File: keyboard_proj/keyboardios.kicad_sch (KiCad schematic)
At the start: 23 parts

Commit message: Tous les schematics vérifiés 1x
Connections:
- net PB0: now also J?.19 (Pin_19); no longer J?.17 (Pin_17)
- net PB2: now also J?.17 (Pin_17); no longer J?.19 (Pin_19)
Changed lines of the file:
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@@
     )
   )
-  (global_label "PB0" (shape input) (at 154.94 129.54 90) (fields_autoplaced)
+  (global_label "PB0" (shape input) (at 149.86 129.54 90) (fields_autoplaced)
     (effects (font (size 1.27 1.27)) (justify left))
-    (property "Intersheet References" "${INTERSHEET_REFS}" (id 0) (at 155.0194 123.3774 90)
+    (property "Intersheet References" "${INTERSHEET_REFS}" (id 0) (at 149.9394 123.3774 90)
       (effects (font (size 1.27 1.27)) (justify left) hide)
     )
@@
     )
   )
-  (global_label "PB2" (shape input) (at 149.86 129.54 90) (fields_autoplaced)
+  (global_label "PB2" (shape input) (at 154.94 129.54 90) (fields_autoplaced)
     (effects (font (size 1.27 1.27)) (justify left))
-    (property "Intersheet References" "${INTERSHEET_REFS}" (id 0) (at 149.9394 123.3774 90)
+    (property "Intersheet References" "${INTERSHEET_REFS}" (id 0) (at 155.0194 123.3774 90)
       (effects (font (size 1.27 1.27)) (justify left) hide)
     )

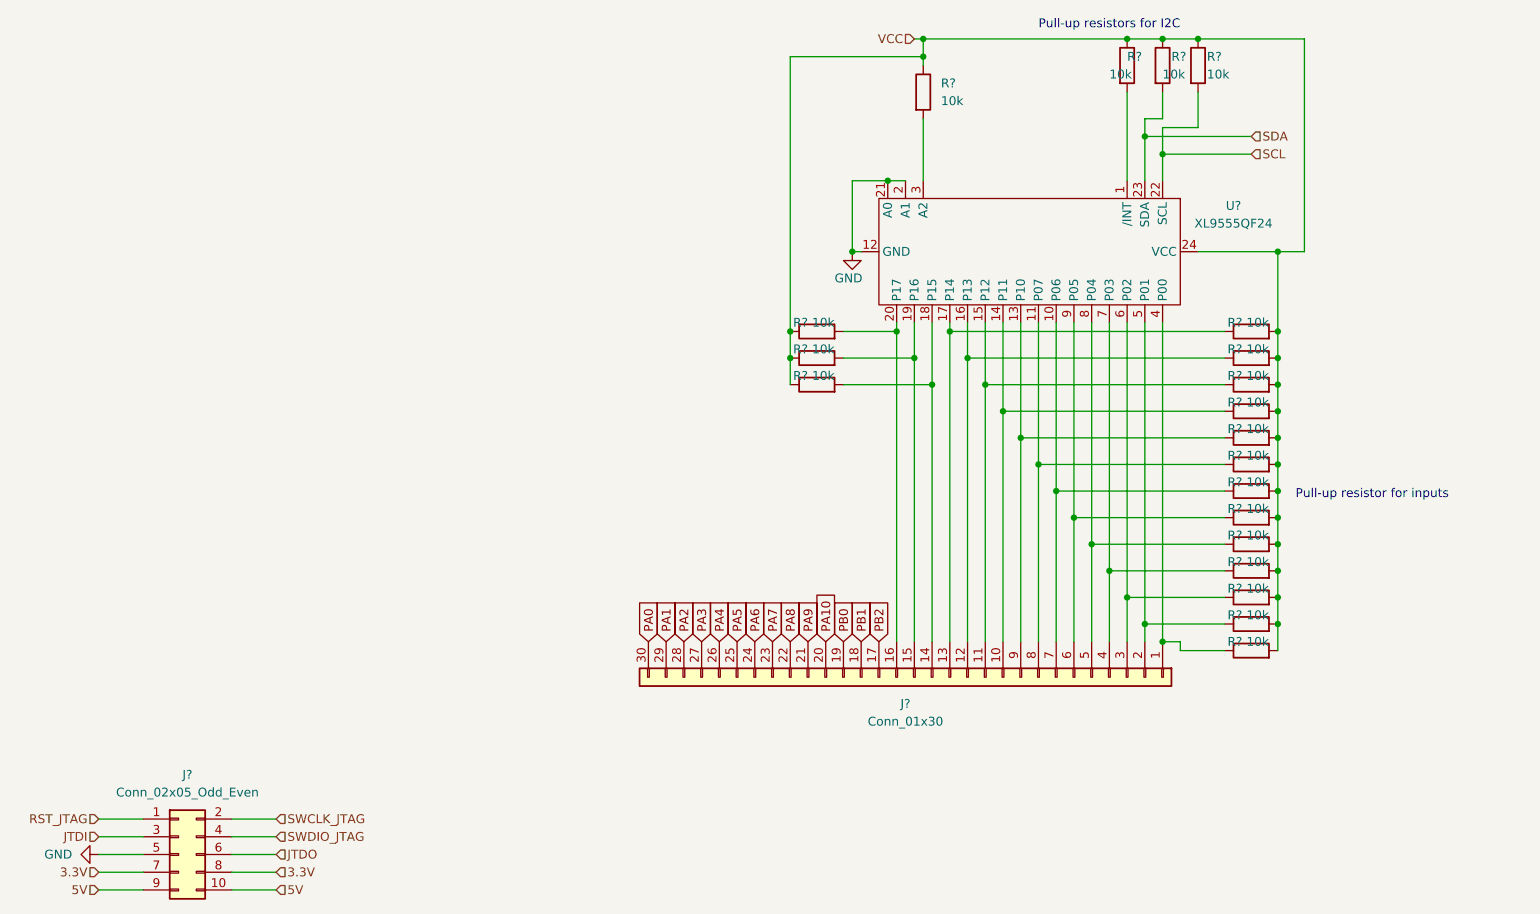
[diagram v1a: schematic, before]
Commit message: Ajout backlight et light sensor (in progress)
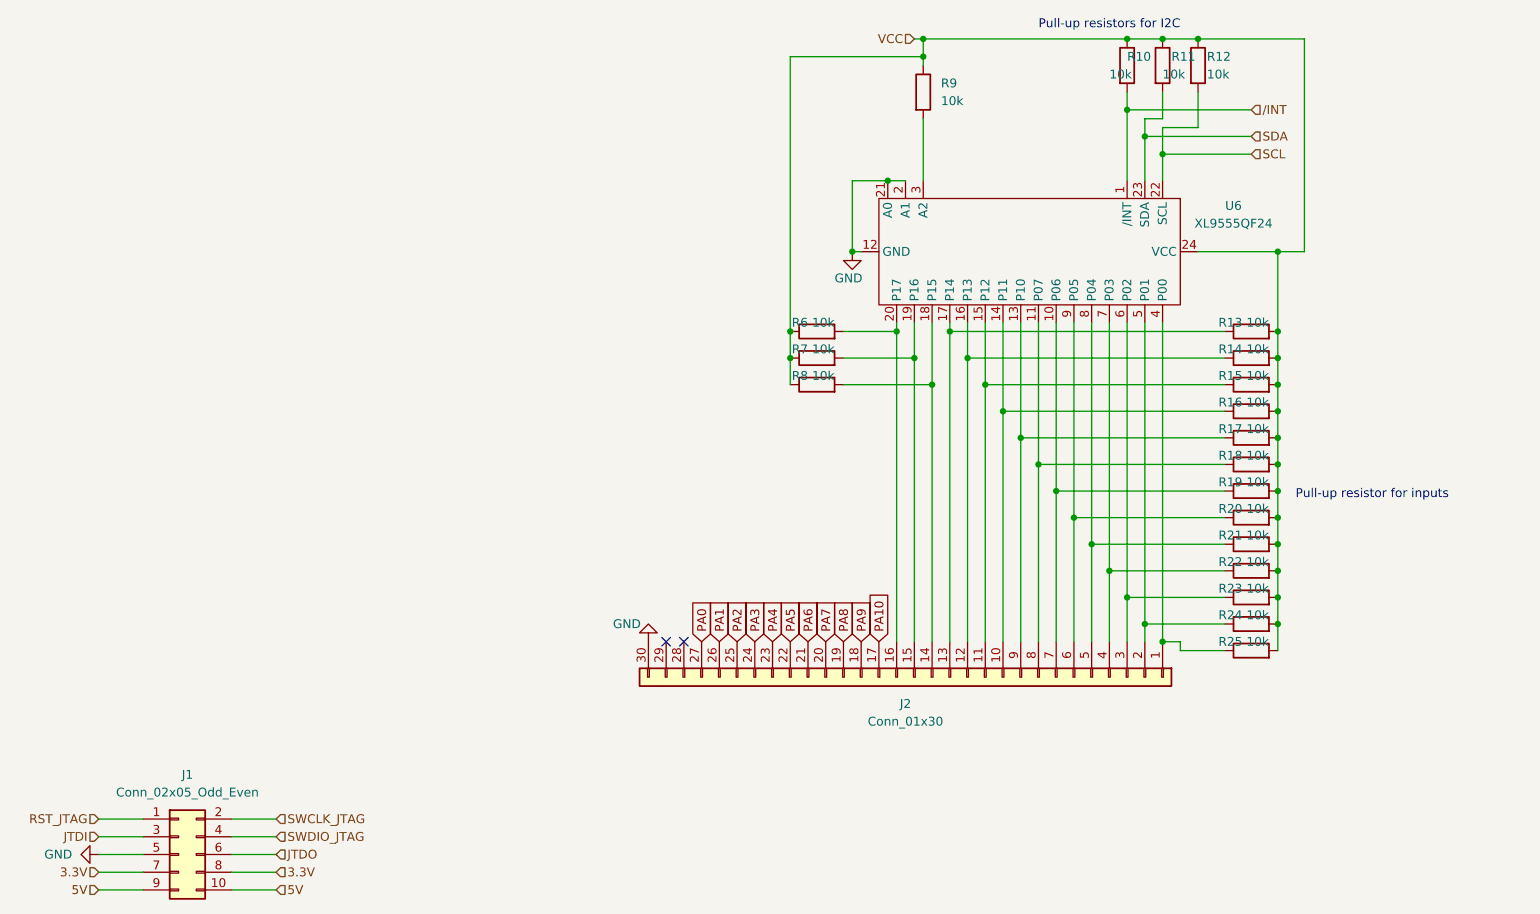
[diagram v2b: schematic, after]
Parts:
- gave numbers to parts that had none: 23
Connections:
- net PB0 is gone; now on net PA8: J2.19 (Pin_19)
- net PB1 is gone; now on net PA9: J2.18 (Pin_18)
- net PB2 is gone; now on net PA10: J2.17 (Pin_17)
- net GND: now also J2.30 (Pin_30)
- net PA0: now also J2.27 (Pin_27); no longer J2.30 (Pin_30)
- net PA1: now also J2.26 (Pin_26); no longer J2.29 (Pin_29)
- net PA10: no longer J2.20 (Pin_20)
- net PA2: now also J2.25 (Pin_25); no longer J2.28 (Pin_28)
- net PA3: now also J2.24 (Pin_24); no longer J2.27 (Pin_27)
- net PA4: now also J2.23 (Pin_23); no longer J2.26 (Pin_26)
- net PA5: now also J2.22 (Pin_22); no longer J2.25 (Pin_25)
- net PA6: now also J2.21 (Pin_21); no longer J2.24 (Pin_24)
- net PA7: now also J2.20 (Pin_20); no longer J2.23 (Pin_23)
- net PA8: no longer J2.22 (Pin_22)
- net PA9: no longer J2.21 (Pin_21)
- net /INT: now reaches R10.2, U6.1 (/INT)
- no-connect marks 0 -> 2

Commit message: Ajout des empreintes, il en manque encore
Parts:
- R10, R11, R12, R13, R14, R15, R16, R17, R18, R19, R20, R21, R22, R23, R24, R25, R6, R7, R8, R9: footprint (none) -> Resistor_SMD:R_0402_1005Metric
- U6: footprint (none) -> Package_DFN_QFN:QFN-24-1EP_4x4mm_P0.5mm_EP2.7x2.7mm
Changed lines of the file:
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@@
       (effects (font (size 1.27 1.27)) (justify left))
     )
-    (property "Footprint" "" (id 2) (at 193.802 46.99 90)
+    (property "Footprint" "Resistor_SMD:R_0402_1005Metric" (id 2) (at 193.802 46.99 90)
       (effects (font (size 1.27 1.27)) hide)
     )
@@
       (effects (font (size 1.27 1.27)) (justify left))
     )
-    (property "Footprint" "" (id 2) (at 208.28 102.108 90)
+    (property "Footprint" "Resistor_SMD:R_0402_1005Metric" (id 2) (at 208.28 102.108 90)
       (effects (font (size 1.27 1.27)) hide)
     )
@@
       (effects (font (size 1.27 1.27)) (justify left))
     )
-    (property "Footprint" "" (id 2) (at 188.722 46.99 90)
+    (property "Footprint" "Resistor_SMD:R_0402_1005Metric" (id 2) (at 188.722 46.99 90)
       (effects (font (size 1.27 1.27)) hide)
     )
@@
       (effects (font (size 1.27 1.27)) (justify left))
     )
-    (property "Footprint" "" (id 2) (at 208.28 98.298 90)
+    (property "Footprint" "Resistor_SMD:R_0402_1005Metric" (id 2) (at 208.28 98.298 90)
       (effects (font (size 1.27 1.27)) hide)
     )
@@
       (effects (font (size 1.27 1.27)) (justify left))
     )
-    (property "Footprint" "" (id 2) (at 159.512 50.8 90)
+    (property "Footprint" "Resistor_SMD:R_0402_1005Metric" (id 2) (at 159.512 50.8 90)
       (effects (font (size 1.27 1.27)) hide)
     )
@@
       (effects (font (size 1.27 1.27)) (justify left))
     )
-    (property "Footprint" "" (id 2) (at 208.28 94.488 90)
+    (property "Footprint" "Resistor_SMD:R_0402_1005Metric" (id 2) (at 208.28 94.488 90)
       (effects (font (size 1.27 1.27)) hide)
     )
@@
       (effects (font (size 1.27 1.27)) (justify left))
     )
-    (property "Footprint" "" (id 2) (at 208.28 86.868 90)
+    (property "Footprint" "Resistor_SMD:R_0402_1005Metric" (id 2) (at 208.28 86.868 90)
       (effects (font (size 1.27 1.27)) hide)
     )
@@
       (effects (font (size 1.27 1.27)) (justify left))
     )
-    (property "Footprint" "" (id 2) (at 208.28 121.158 90)
+    (property "Footprint" "Resistor_SMD:R_0402_1005Metric" (id 2) (at 208.28 121.158 90)
       (effects (font (size 1.27 1.27)) hide)
     )
@@
       (effects (font (size 1.27 1.27)) (justify left))
     )
-    (property "Footprint" "" (id 2) (at 208.28 132.588 90)
+    (property "Footprint" "Resistor_SMD:R_0402_1005Metric" (id 2) (at 208.28 132.588 90)
       (effects (font (size 1.27 1.27)) hide)
     )
@@
       (effects (font (size 1.27 1.27)) (justify left))
     )
-    (property "Footprint" "" (id 2) (at 208.28 90.678 90)
+    (property "Footprint" "Resistor_SMD:R_0402_1005Metric" (id 2) (at 208.28 90.678 90)
       (effects (font (size 1.27 1.27)) hide)
     )
@@
       (effects (font (size 1.27 1.27)) (justify left))
     )
-    (property "Footprint" "" (id 2) (at 208.28 109.728 90)
+    (property "Footprint" "Resistor_SMD:R_0402_1005Metric" (id 2) (at 208.28 109.728 90)
       (effects (font (size 1.27 1.27)) hide)
     )
@@
       (effects (font (size 1.27 1.27)) (justify left))
     )
-    (property "Footprint" "" (id 2) (at 208.28 117.348 90)
+    (property "Footprint" "Resistor_SMD:R_0402_1005Metric" (id 2) (at 208.28 117.348 90)
       (effects (font (size 1.27 1.27)) hide)
     )
@@
       (effects (font (size 1.27 1.27)) (justify left))
     )
-    (property "Footprint" "" (id 2) (at 208.28 113.538 90)
+    (property "Footprint" "Resistor_SMD:R_0402_1005Metric" (id 2) (at 208.28 113.538 90)
       (effects (font (size 1.27 1.27)) hide)
     )
@@
       (effects (font (size 1.27 1.27)) (justify left))
     )
-    (property "Footprint" "" (id 2) (at 208.28 105.918 90)
+    (property "Footprint" "Resistor_SMD:R_0402_1005Metric" (id 2) (at 208.28 105.918 90)
       (effects (font (size 1.27 1.27)) hide)
     )
@@
     (property "Reference" "U6" (id 0) (at 205.74 67.0812 90))
     (property "Value" "XL9555QF24" (id 1) (at 205.74 69.6212 90))
-    (property "Footprint" "" (id 2) (at 191.77 73.66 0)
+    (property "Footprint" "Package_DFN_QFN:QFN-24-1EP_4x4mm_P0.5mm_EP2.7x2.7mm" (id 2) (at 191.77 73.66 0)
       (effects (font (size 1.27 1.27)) hide)
     )
@@
       (effects (font (size 1.27 1.27)) (justify left))
     )
-    (property "Footprint" "" (id 2) (at 146.05 86.868 90)
+    (property "Footprint" "Resistor_SMD:R_0402_1005Metric" (id 2) (at 146.05 86.868 90)
       (effects (font (size 1.27 1.27)) hide)
     )
@@
       (effects (font (size 1.27 1.27)) (justify left))
     )
-    (property "Footprint" "" (id 2) (at 208.28 128.778 90)
+    (property "Footprint" "Resistor_SMD:R_0402_1005Metric" (id 2) (at 208.28 128.778 90)
       (effects (font (size 1.27 1.27)) hide)
     )
@@
       (effects (font (size 1.27 1.27)) (justify left))
     )
-    (property "Footprint" "" (id 2) (at 146.05 90.678 90)
+    (property "Footprint" "Resistor_SMD:R_0402_1005Metric" (id 2) (at 146.05 90.678 90)
       (effects (font (size 1.27 1.27)) hide)
     )
@@
       (effects (font (size 1.27 1.27)) (justify left))
     )
-    (property "Footprint" "" (id 2) (at 198.882 46.99 90)
+    (property "Footprint" "Resistor_SMD:R_0402_1005Metric" (id 2) (at 198.882 46.99 90)
       (effects (font (size 1.27 1.27)) hide)
     )
@@
       (effects (font (size 1.27 1.27)) (justify left))
     )
-    (property "Footprint" "" (id 2) (at 146.05 94.488 90)
+    (property "Footprint" "Resistor_SMD:R_0402_1005Metric" (id 2) (at 146.05 94.488 90)
       (effects (font (size 1.27 1.27)) hide)
     )
@@
       (effects (font (size 1.27 1.27)) (justify left))
     )
-    (property "Footprint" "" (id 2) (at 208.28 124.968 90)
-      (effects (font (size 1.27 1.27)) hide)
-    )
+    (property "Footprint" "Resistor_SMD:R_0402_1005Metric" (id 2) (at 208.28 124.968 90)
+      (effects (font (size 1.27 1.27)) hide)
+    )

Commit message: Empreintes finies, besoin de reverifier, disposition des composants sur la carte
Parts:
- removed J1: Conn_02x05_Odd_Even, symbol Connector_Generic:Conn_02x05_Odd_Even
- removed J2: Conn_01x30, symbol Connector_Generic:Conn_01x30
- added J1: Conn_02x04_Odd_Even, SamacSys_Parts:debug_conn, symbol Connector_Generic:Conn_02x04_Odd_Even
- added J2: Conn_01x32, SamacSys_Parts:conn_keyboard, symbol Connector_Generic:Conn_01x32
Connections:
- net 3.3V: now also J1.7 (Pin_7)
- net 5V: now also J1.8 (Pin_8)
- net GND: now also J1.5 (Pin_5), J2.28 (Pin_28), J2.29 (Pin_29), J2.30 (Pin_30), J2.31 (Pin_31), J2.32 (Pin_32)
- net JTDI: now also J1.3 (Pin_3)
- net JTDO: now also J1.6 (Pin_6)
- net PA0: now also J2.27 (Pin_27)
- net PA1: now also J2.26 (Pin_26)
- net PA10: now also J2.17 (Pin_17)
- net PA2: now also J2.25 (Pin_25)
- net PA3: now also J2.24 (Pin_24)
- net PA4: now also J2.23 (Pin_23)
- net PA5: now also J2.22 (Pin_22)
- net PA6: now also J2.21 (Pin_21)
- net PA7: now also J2.20 (Pin_20)
- net PA8: now also J2.19 (Pin_19)
- net PA9: now also J2.18 (Pin_18)
- net RST_JTAG: now also J1.1 (Pin_1)
- net SWCLK_JTAG: now also J1.2 (Pin_2)
- net SWDIO_JTAG: now also J1.4 (Pin_4)
- net at R17.1, U6.13 (P10): now also J2.9 (Pin_9)
- net at R16.1, U6.14 (P11): now also J2.10 (Pin_10)
- net at R15.1, U6.15 (P12): now also J2.11 (Pin_11)
- net at R13.1, U6.17 (P14): now also J2.13 (Pin_13)
- net at R22.1, U6.7 (P03): now also J2.4 (Pin_4)
- net at R25.1, U6.4 (P00): now also J2.1 (Pin_1)
- net at R14.1, U6.16 (P13): now also J2.12 (Pin_12)
- net at R19.1, U6.10 (P06): now also J2.7 (Pin_7)
- net at R21.1, U6.8 (P04): now also J2.5 (Pin_5)
- net at R20.1, U6.9 (P05): now also J2.6 (Pin_6)
- net at R18.1, U6.11 (P07): now also J2.8 (Pin_8)
- net at R8.2, U6.18 (P15): now also J2.14 (Pin_14)
- net at R7.2, U6.19 (P16): now also J2.15 (Pin_15)
- net at R6.2, U6.20 (P17): now also J2.16 (Pin_16)
- net at R24.1, U6.5 (P01): now also J2.2 (Pin_2)
- net at R23.1, U6.6 (P02): now also J2.3 (Pin_3)
- no-connect marks 2 -> 0

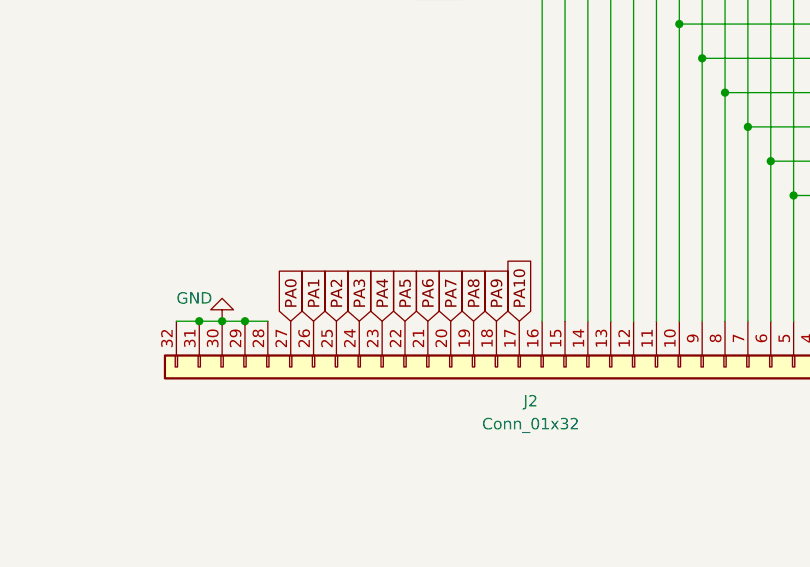
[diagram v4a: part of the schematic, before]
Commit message: passage kicad 7, routing bien avancé
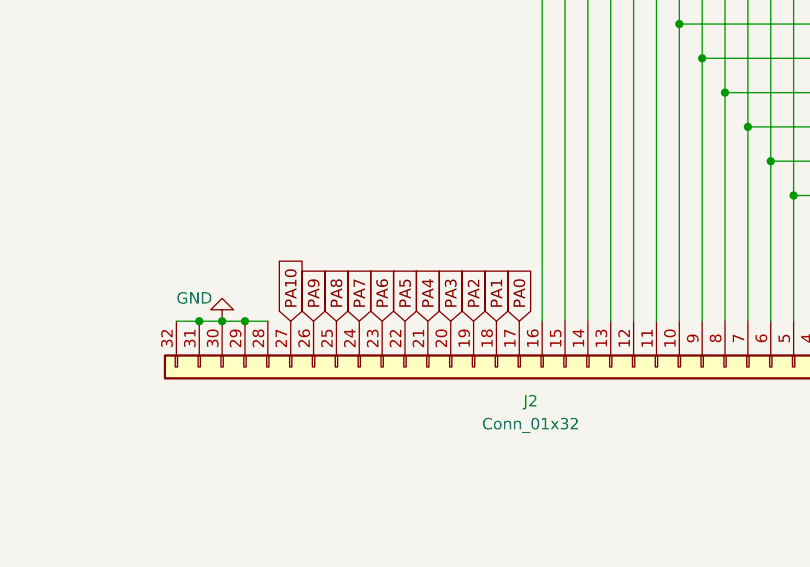
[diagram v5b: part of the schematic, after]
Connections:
- net PA0: now also J2.17 (Pin_17); no longer J2.27 (Pin_27)
- net PA1: now also J2.18 (Pin_18); no longer J2.26 (Pin_26)
- net PA10: now also J2.27 (Pin_27); no longer J2.17 (Pin_17)
- net PA2: now also J2.19 (Pin_19); no longer J2.25 (Pin_25)
- net PA3: now also J2.20 (Pin_20); no longer J2.24 (Pin_24)
- net PA4: now also J2.21 (Pin_21); no longer J2.23 (Pin_23)
- net PA6: now also J2.23 (Pin_23); no longer J2.21 (Pin_21)
- net PA7: now also J2.24 (Pin_24); no longer J2.20 (Pin_20)
- net PA8: now also J2.25 (Pin_25); no longer J2.19 (Pin_19)
- net PA9: now also J2.26 (Pin_26); no longer J2.18 (Pin_18)

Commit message: PCB bien avancé, presque fini mais je dois selectionner des pieces de jlcpcb pour baisser les couts
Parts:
- J1: LCSC (none) -> C376087
- J2: LCSC (none) -> C2842545
- R10, R11, R12, R13, R14, R15, R16, R17, R18, R19, R20, R21, R22, R23, R24, R25, R6, R7, R8, R9: LCSC (none) -> C2692697
- U6: LCSC (none) -> C5125492
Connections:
- net SCL: now also R12.1; no longer R12.2
- net SDA: now also R11.1; no longer R11.2
- net VCC: now also R10.2, R11.2, R12.2, R9.2; no longer R10.1, R11.1, R12.1, R9.1
- net /INT: now also R10.1; no longer R10.2
- net at U6.3 (A2): now also R9.1; no longer R9.2
